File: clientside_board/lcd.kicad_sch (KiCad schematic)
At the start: 14 parts, among them J11 LCD Connector, J12 Potentiometer Connector, U8 SN74LVC8T245, U9 SN74LVC8T245

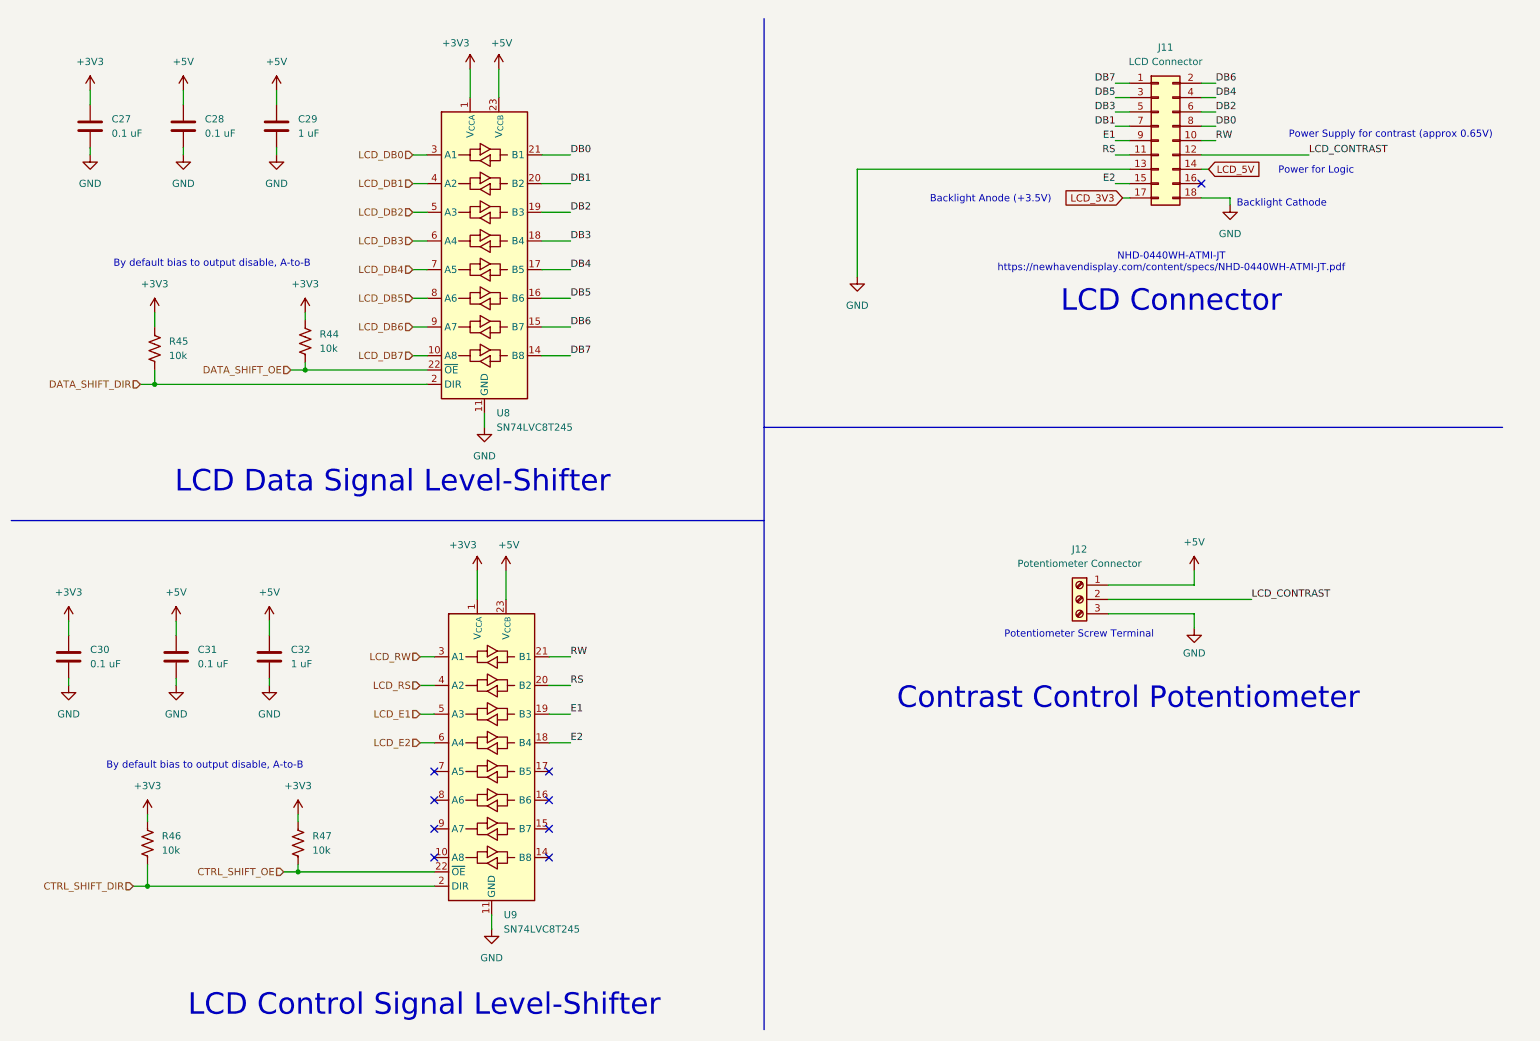
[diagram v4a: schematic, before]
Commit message: Update power for 5V LCD display
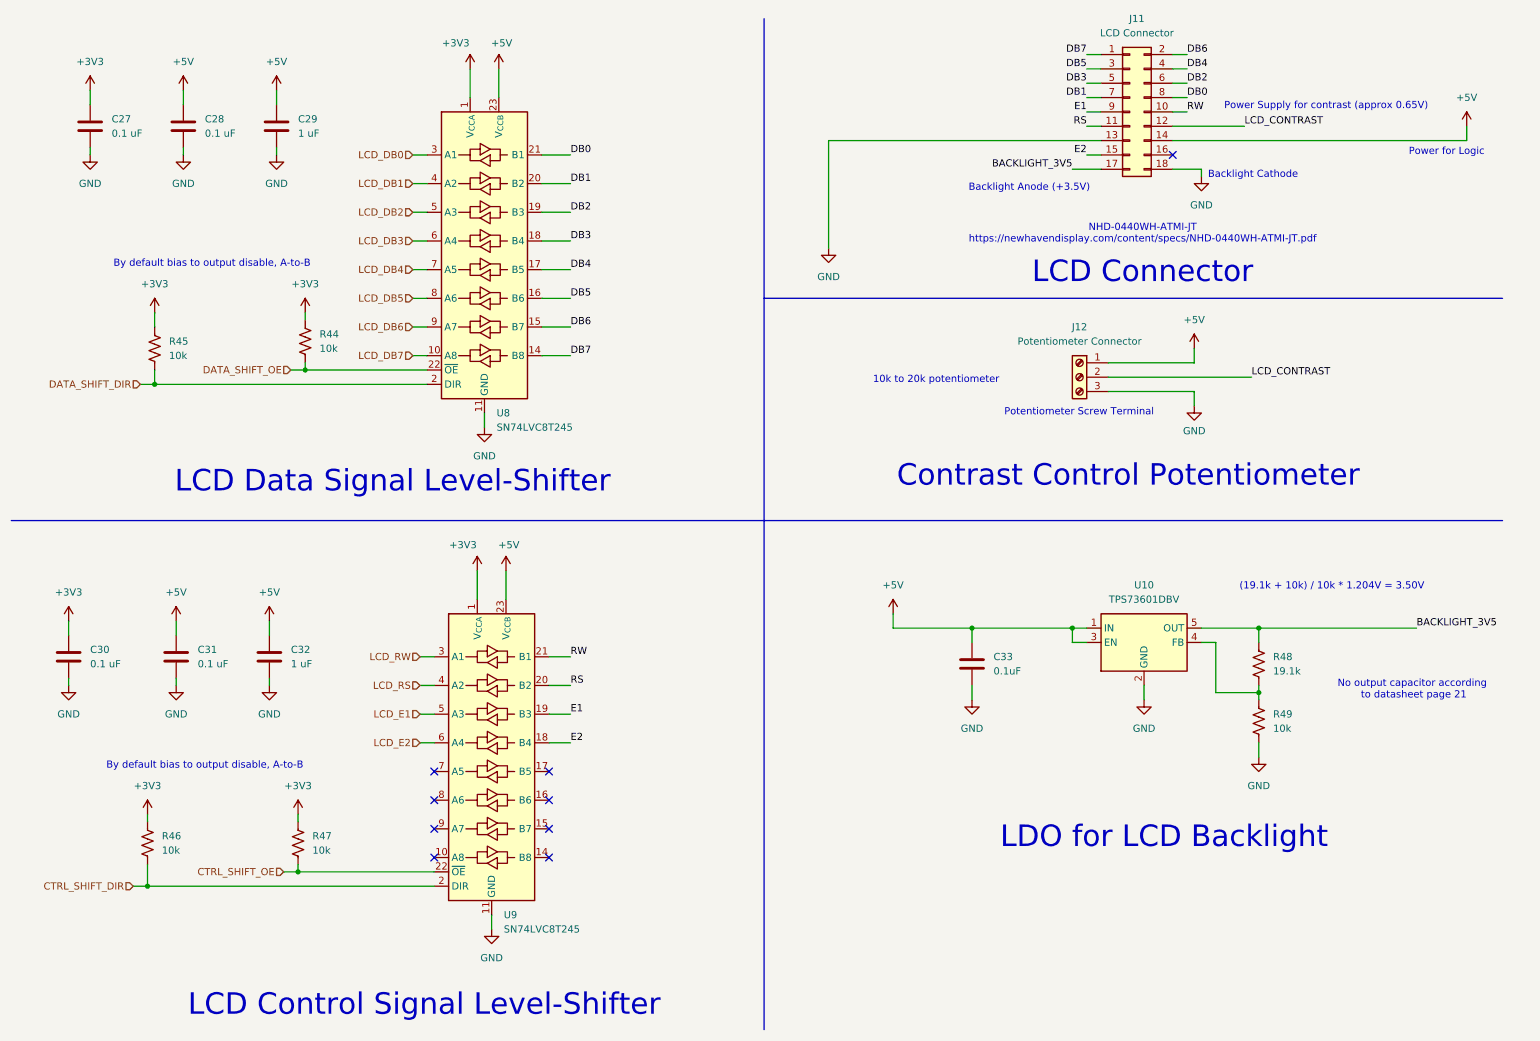
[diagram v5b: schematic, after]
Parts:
- added C33: 0.1uF, symbol Device:C
- added R48: 19.1k, symbol Device:R_US
- added R49: 10k, symbol Device:R_US
- added U10: TPS73601DBV, Package_TO_SOT_SMD:SOT-23-5, symbol Regulator_Linear:TPS73601DBV
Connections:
- net LCD_5V is gone; now on net +5V: J11.14 (Pin_14)
- net +5V: now also C33.1, U10.1 (IN), U10.3 (EN)
- net GND: now also C33.2, R49.2, U10.2 (GND)
- net LCD_3V3 renamed BACKLIGHT_3V5
- net BACKLIGHT_3V5: now also R48.1, U10.5 (OUT)
- new net: R48.2, R49.1, U10.4 (FB)
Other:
- note added: "(19.1k + 10k) / 10k * 1.204V = 3.50V"
- note added: "10k to 20k potentiometer"
- note added: "LDO for LCD Backlight"
- note added: "No output capacitor according to datasheet page 21"
- moved on the sheet: J11, J12

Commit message: Top sheet update
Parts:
- C21: renamed from C30; footprint (none) -> Capacitor_SMD:C_0603_1608Metric_Pad1.08x0.95mm_HandSolder
- C22: renamed from C27; footprint (none) -> Capacitor_SMD:C_0603_1608Metric_Pad1.08x0.95mm_HandSolder
- C23: renamed from C31; footprint (none) -> Capacitor_SMD:C_0603_1608Metric_Pad1.08x0.95mm_HandSolder
- C24: renamed from C28; footprint (none) -> Capacitor_SMD:C_0603_1608Metric_Pad1.08x0.95mm_HandSolder
- C25: renamed from C32; footprint (none) -> Capacitor_SMD:C_0603_1608Metric_Pad1.08x0.95mm_HandSolder
- C26: renamed from C29; footprint (none) -> Capacitor_SMD:C_0603_1608Metric_Pad1.08x0.95mm_HandSolder
- C27: renamed from C33; footprint (none) -> Capacitor_SMD:C_0603_1608Metric_Pad1.08x0.95mm_HandSolder
- renumbered J12 to J11, J11 to J12, R46 to R32, R45 to R33, R47 to R34, R44 to R35, R48 to R36, R49 to R37, U8 to U3, U9 to U4, U10 to U5
